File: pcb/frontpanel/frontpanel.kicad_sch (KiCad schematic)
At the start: 9 parts, among them J1 xx, J2 xx, J3 xx, J4 xx

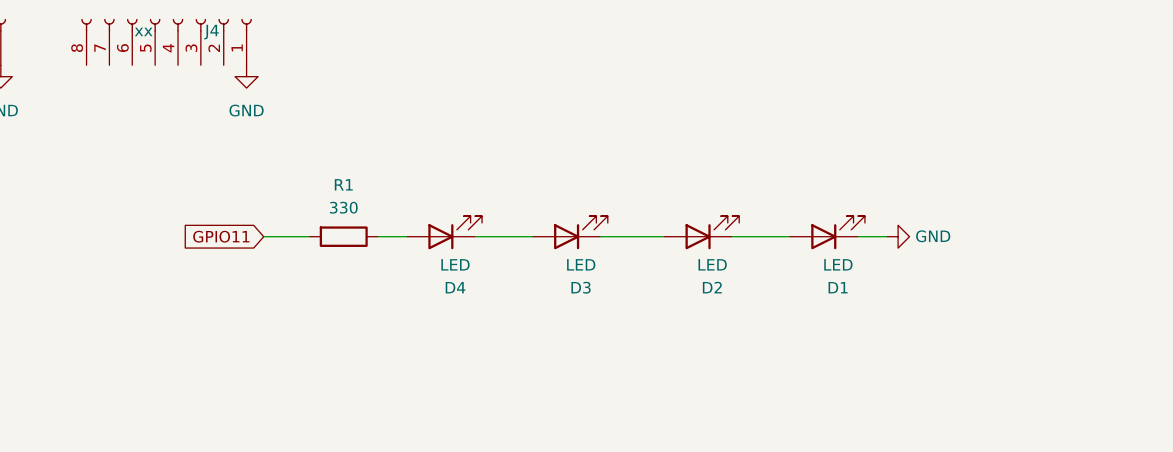
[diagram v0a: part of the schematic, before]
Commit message: [pcb] update frontpanel (mostly, leds)
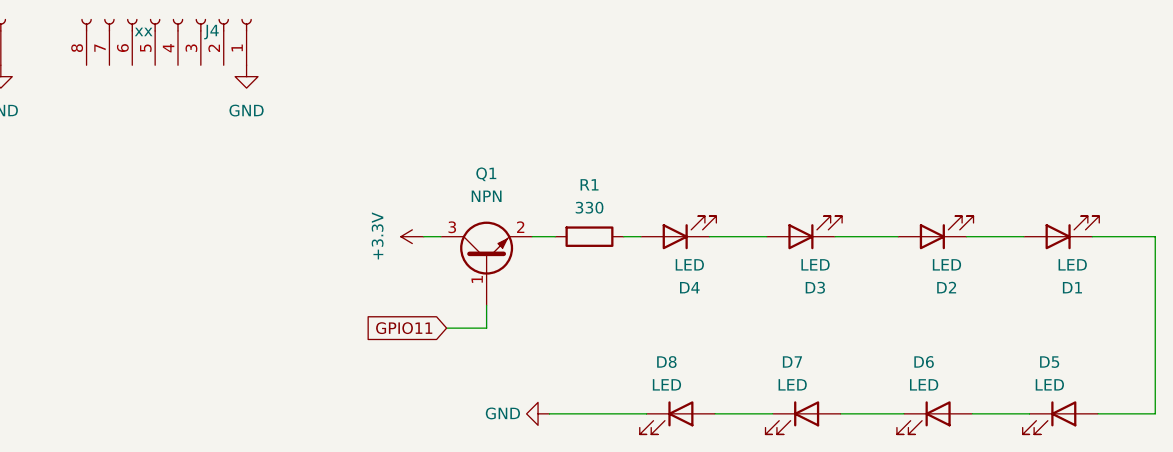
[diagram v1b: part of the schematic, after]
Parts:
- added D5, D6, D7, D8: LED, LED_SMD:LED_0805_2012Metric, symbol Device:LED
- added Q1: NPN, Package_TO_SOT_SMD:SOT-23, symbol Transistor_BJT:BC817
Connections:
- net +3.3V: now also Q1.3 (C)
- net GND: now also D8.1 (K); no longer D1.1 (K)
- net GPIO11: now also Q1.1 (B); no longer R1.2
- new net: Q1.2 (E), R1.2
- new net: D5.1 (K), D6.2 (A)
- new net: D1.1 (K), D5.2 (A)
- new net: D6.1 (K), D7.2 (A)
- new net: D7.1 (K), D8.2 (A)
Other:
- moved on the sheet: D1, D2, D3, D4

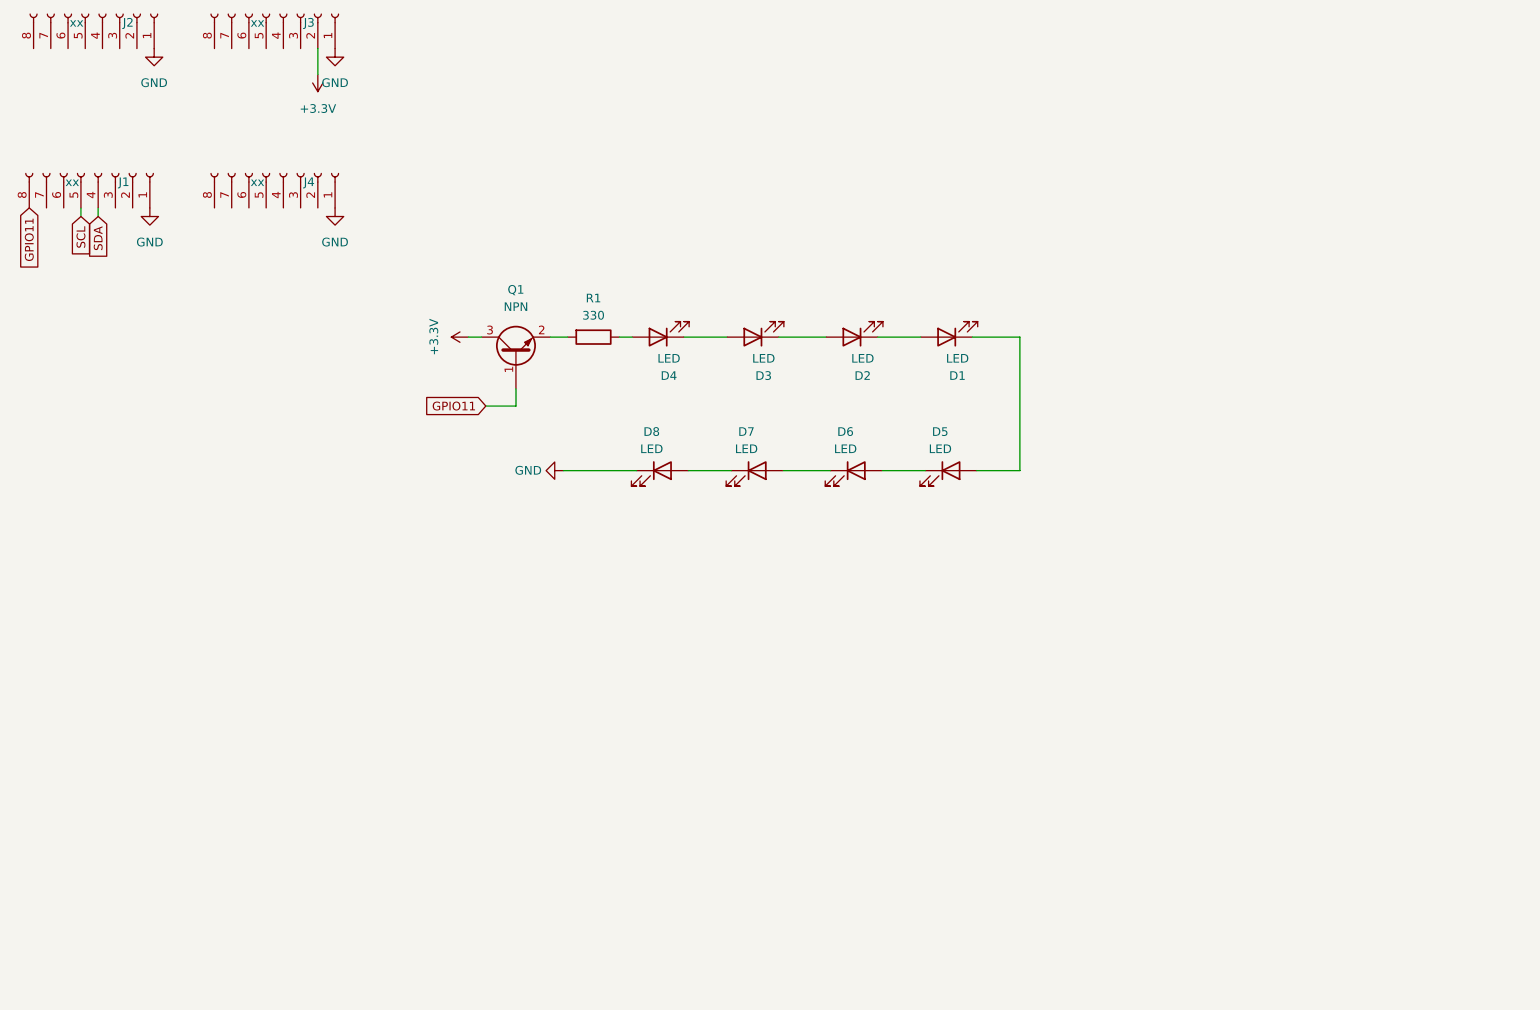
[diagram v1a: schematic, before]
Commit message: [pcb] fix frontpanel pcb LEDs + connexion to main pcb
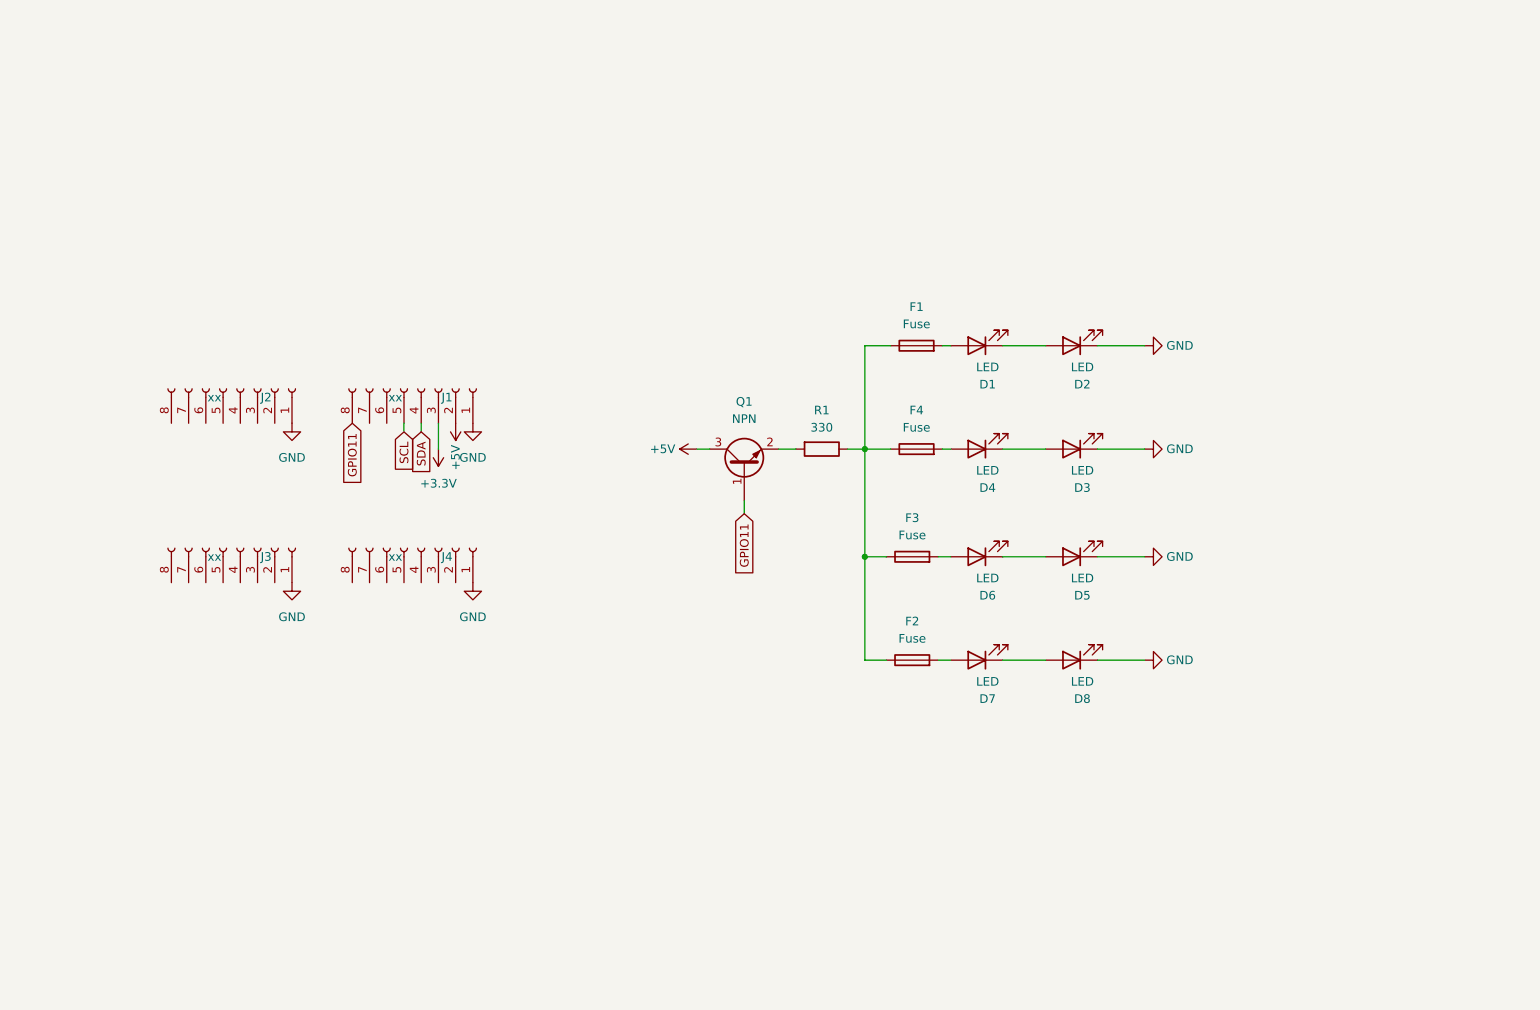
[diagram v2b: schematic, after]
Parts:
- added F1, F2, F3, F4: Fuse, Fuse:Fuse_0805_2012Metric, symbol Device:Fuse
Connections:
- net +3.3V: now also J1.3 (Pin_3); no longer J3.2 (Pin_2), Q1.3 (C)
- net GND: now also D2.1 (K), D3.1 (K), D5.1 (K)
- net at D1.2 (A): now also F1.2; no longer D2.1 (K)
- net at D2.2 (A): now also D1.1 (K); no longer D3.1 (K)
- net at D6.2 (A): now also F3.2; no longer D5.1 (K)
- net at D5.2 (A): now also D6.1 (K); no longer D1.1 (K)
- net at D7.2 (A): now also F2.2; no longer D6.1 (K)
- net at D4.2 (A): now also F4.2; no longer R1.1
- net +5V: now reaches J1.2 (Pin_2)
- net +5V: now also Q1.3 (C)
- new net: F1.1, F2.1, F3.1, F4.1, R1.1
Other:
- moved on the sheet: D3, D4, D7, D8, J1, J2, J3, J4, Q1, R1

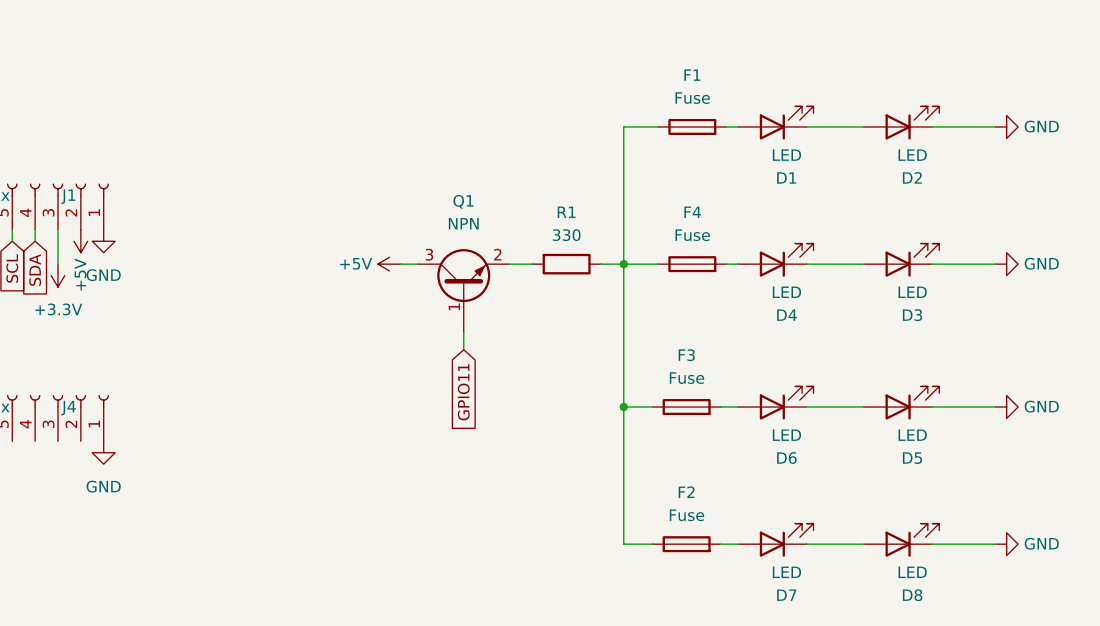
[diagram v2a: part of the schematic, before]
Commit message: [pcb] use optocoupler in frontpanel
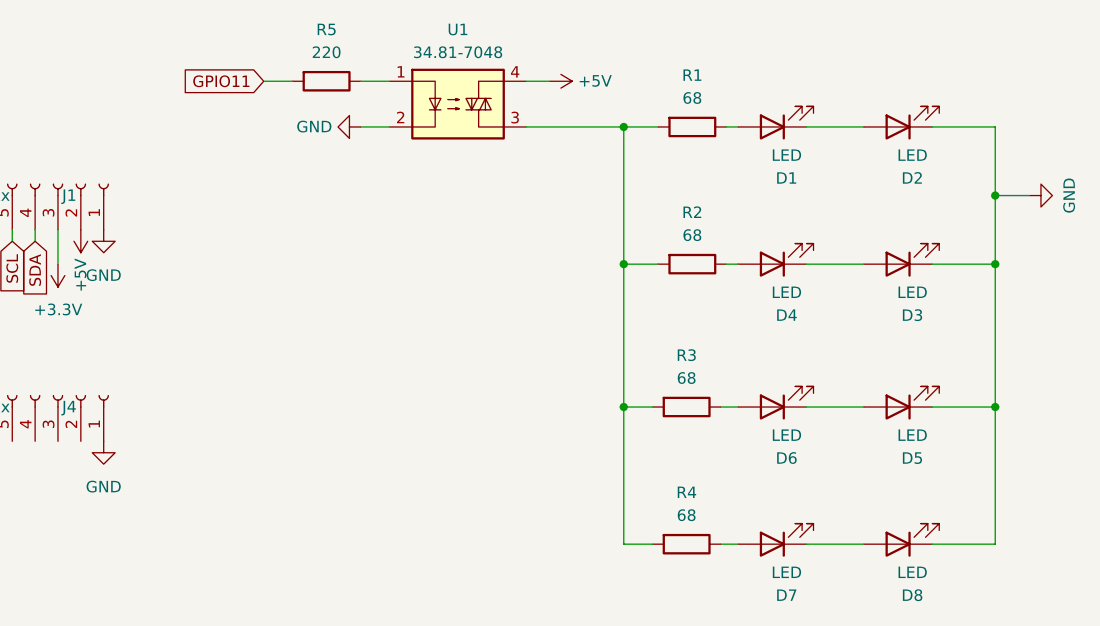
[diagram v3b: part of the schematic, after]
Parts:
- removed F1, F2, F3, F4: Fuse, Fuse:Fuse_0805_2012Metric, symbol Device:Fuse
- removed Q1: NPN, Package_TO_SOT_SMD:SOT-23, symbol Transistor_BJT:BC817
- added R2, R3, R4: 68, Resistor_SMD:R_0603_1608Metric, symbol Device:R
- added R5: 220, Resistor_SMD:R_0603_1608Metric, symbol Device:R
- added U1: 34.81-7048, Package_DIP:SMDIP-4_W7.62mm, symbol Relay_SolidState:FODM3011
- R1: value 330 -> 68
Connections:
- net +5V: now also U1.4
- net GND: now also U1.2
- net GPIO11: now also R5.2
- net at D1.2 (A): now also R1.1
- net at R1.2: now also R2.2, R3.2, R4.2, U1.3
- net at D4.2 (A): now also R2.1
- net at D6.2 (A): now also R3.1
- net at D7.2 (A): now also R4.1
- new net: R5.1, U1.1

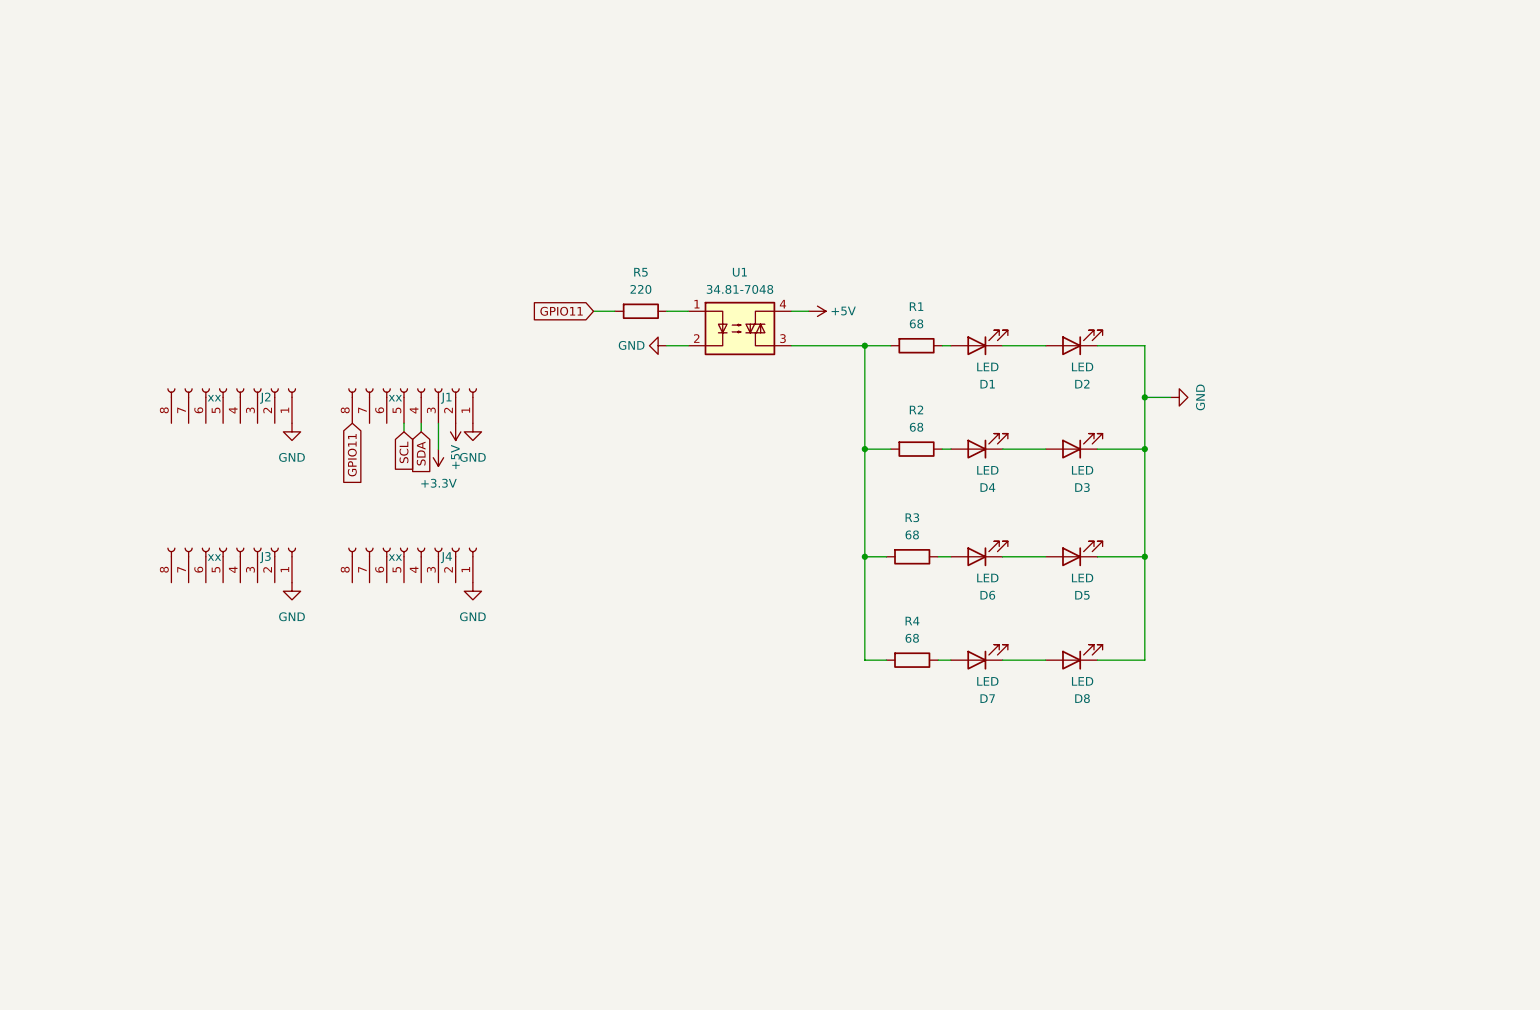
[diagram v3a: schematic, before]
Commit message: [pcb] new GPIO arrangement
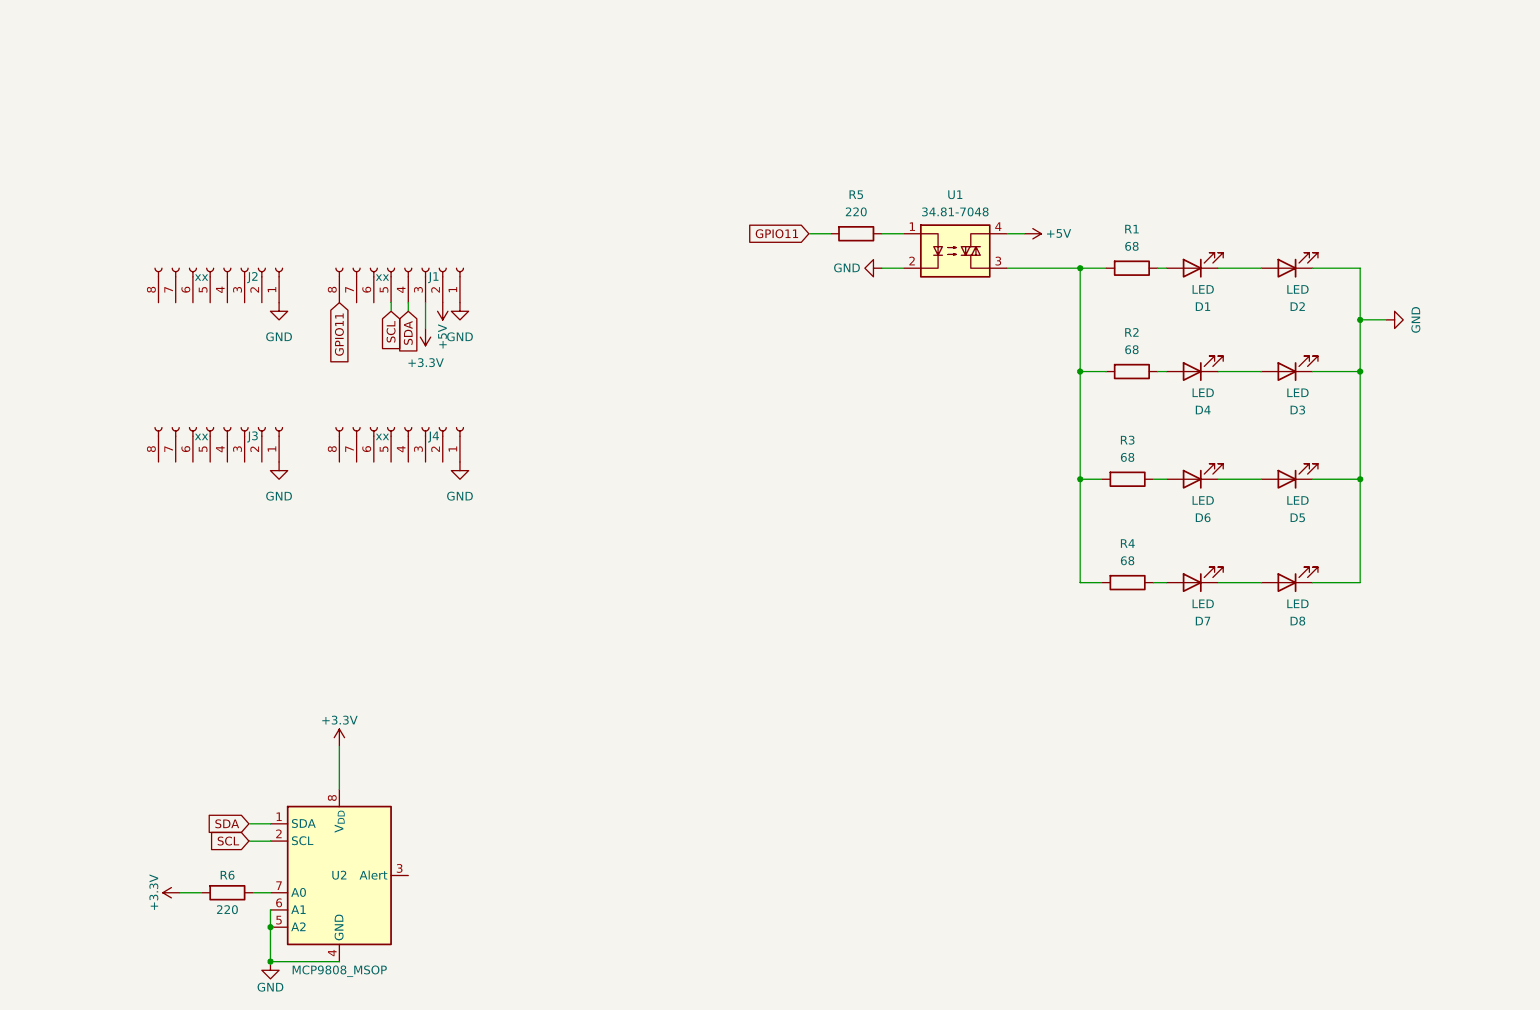
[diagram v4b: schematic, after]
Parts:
- added R6: 220, Resistor_SMD:R_0603_1608Metric, symbol Device:R
- added U2: MCP9808_MSOP, Package_SO:MSOP-8_3x3mm_P0.65mm, symbol Sensor_Temperature:MCP9808_MSOP
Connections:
- net +3.3V: now also R6.2, U2.8 (V_{DD})
- net GND: now also U2.4 (GND), U2.5 (A2), U2.6 (A1)
- net SCL: now also U2.2 (SCL)
- net SDA: now also U2.1 (SDA)
- new net: R6.1, U2.7 (A0)
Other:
- moved on the sheet: D1, D2, D3, D4, D5, D6, D7, D8, J1, J2, J3, J4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
